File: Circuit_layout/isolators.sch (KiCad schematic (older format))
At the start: 0 parts

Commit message: added isolators, as well as voltage meas circuit used by tim
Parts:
- added C? (x6): 0.1u, symbol C
- added C?: DNP, symbol C
- added R? (x5): 2k, symbol R
- added R? (x6): 5k, symbol R
- added R?: 3k, symbol R
- added R? (x2): 4k, symbol R
- added R? (x8): 10k, symbol R
- added R?: 1400, symbol R
- added U? (x3): ACPL-C870, symbol ACPL-C870
- added U? (x3): MCP6004, symbol MCP6004
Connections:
- net labels added: +5V, +5_HV, GND, HV_RTN
- wire segments 0 -> 84
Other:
- note added: "5/4 scaling due to\n0-4V output of I sensor\nConfirm this O/P"
- note added: "Based on 110V (max) from TSV. Planning on putting voltages ~0-2V.\nWhen scaled, will be roughly ~0-5V for ADC read."
- note added: "current meas iso\n"
- note added: "throttle iso"
- note added: "voltage meas iso\n"

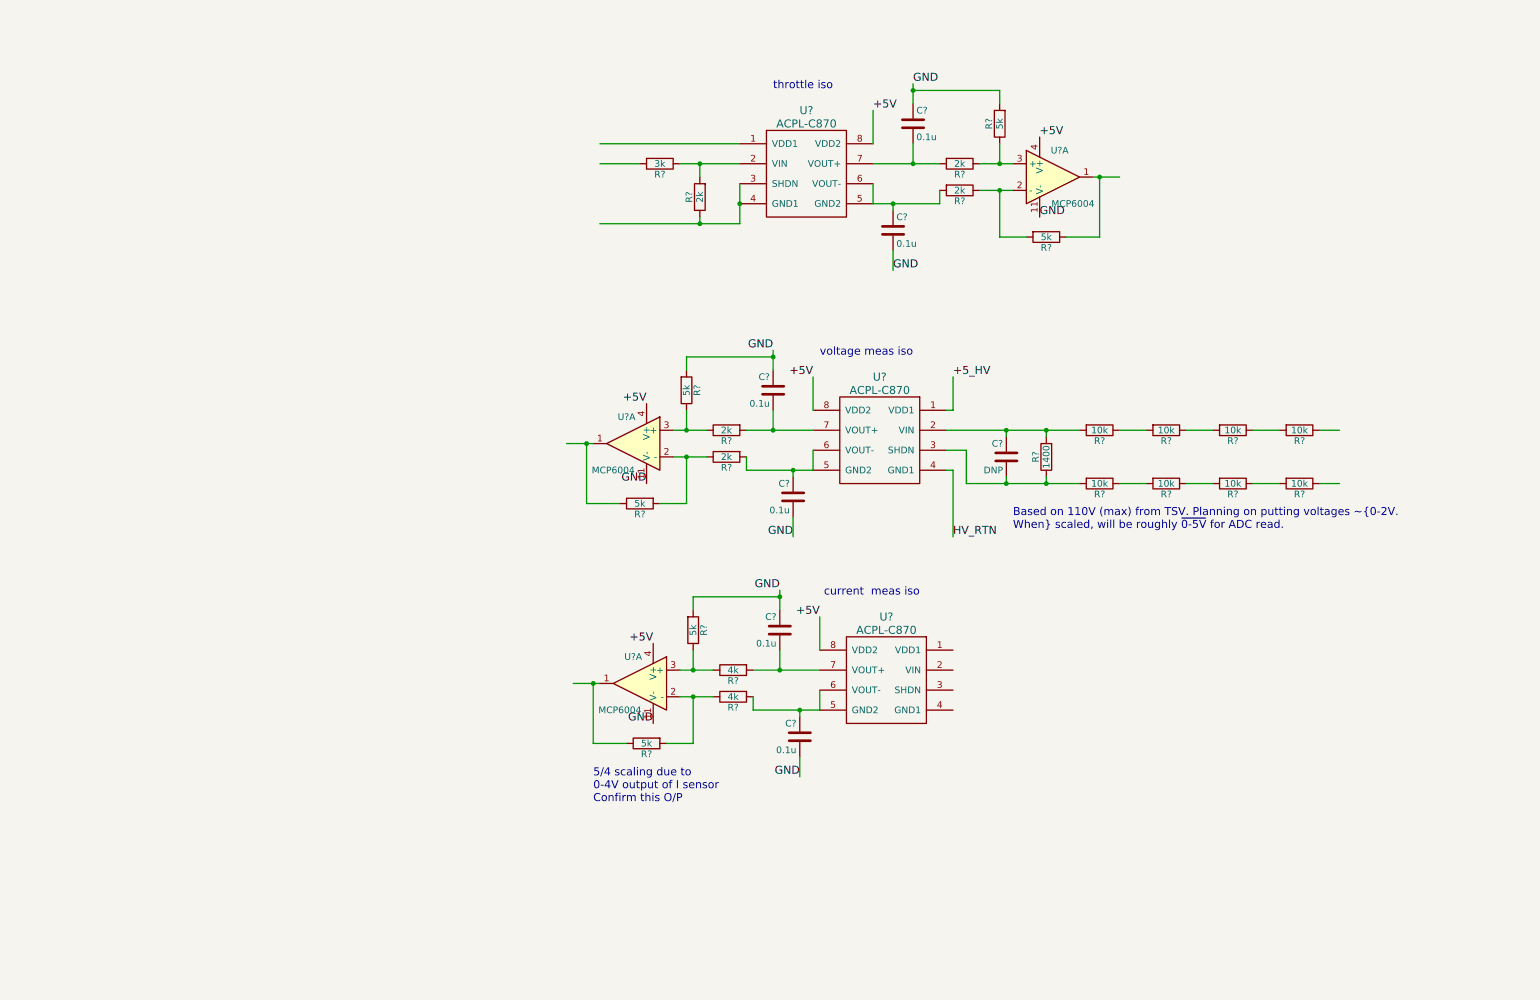
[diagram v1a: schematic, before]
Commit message: added iso circuits, curr. sensor diff amp, IMD fault lt circuit, updated labels
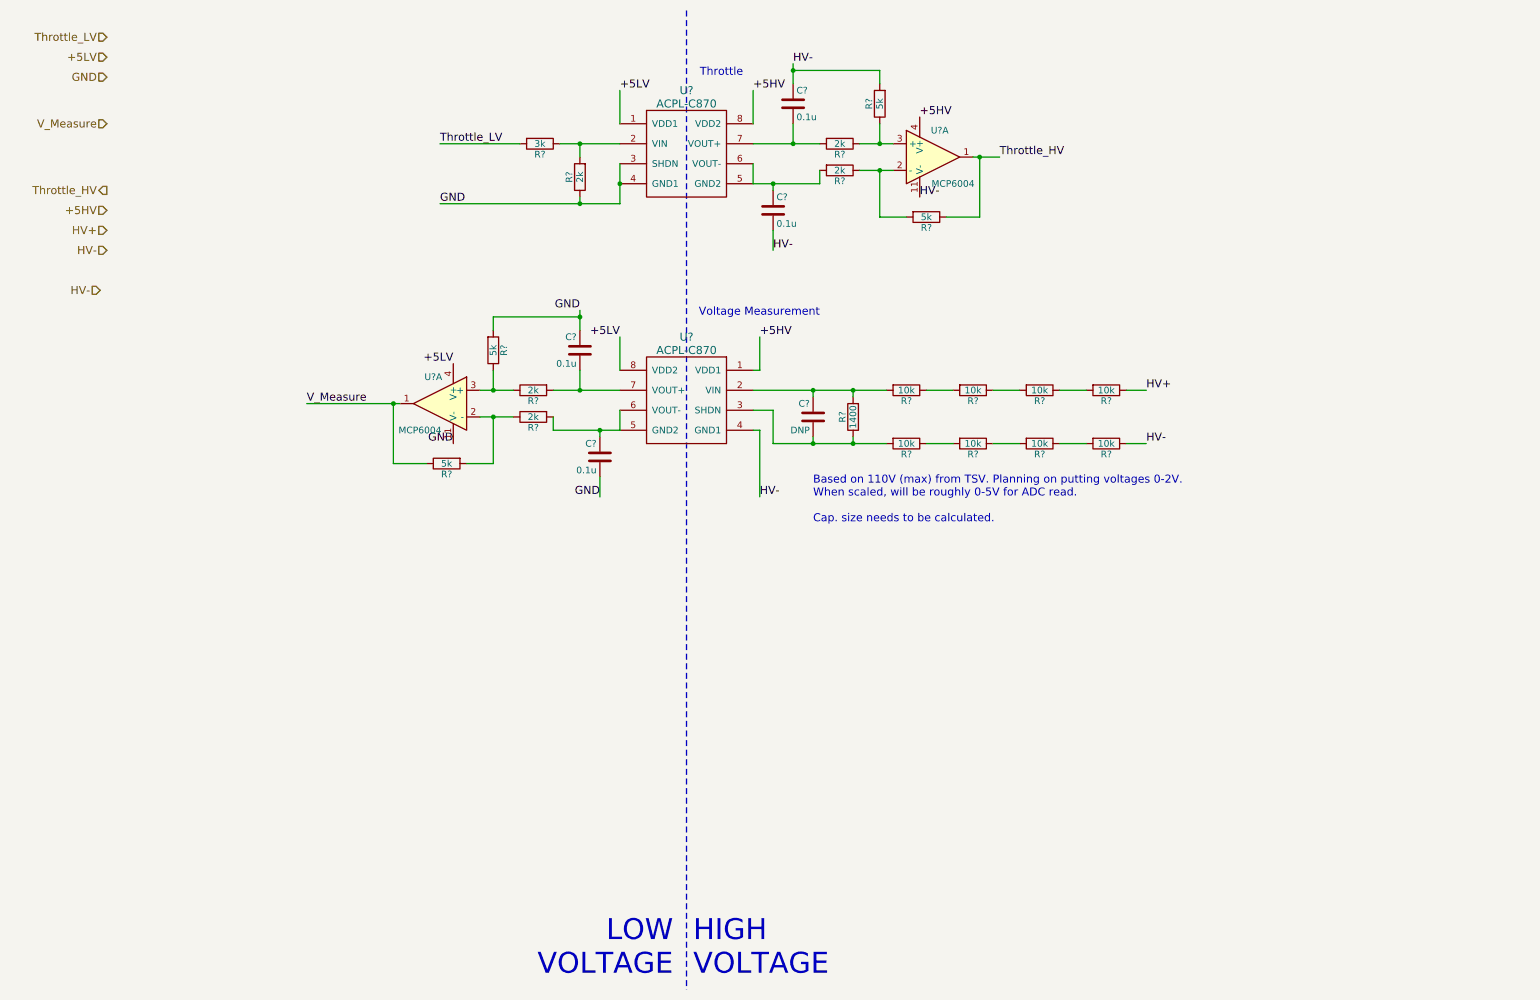
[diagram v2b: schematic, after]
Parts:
- removed C? (x2): 0.1u, symbol C
- removed R? (x2): 4k, symbol R
- removed R? (x2): 5k, symbol R
- removed U?: ACPL-C870, symbol ACPL-C870
- removed U?: MCP6004, symbol MCP6004
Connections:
- net labels added: +5HV, +5LV, HV+, HV-, Throttle_HV, Throttle_LV, V_Measure
- net labels removed: +5V, +5_HV, HV_RTN
- wire segments 84 -> 65
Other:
- note added: "Based on 110V (max) from TSV. Planning on putting voltages 0-2V.\nWhen scaled, will be roughly 0-5V for ADC read.\n\nCap. size needs to be calculated."
- note added: "HIGH\nVOLTAGE"
- note added: "LOW\nVOLTAGE"
- note added: "Throttle"
- note added: "Voltage Measurement"
- note removed: "5/4 scaling due to\n0-4V output of I sensor\nConfirm this O/P"
- note removed: "Based on 110V (max) from TSV. Planning on putting voltages ~0-2V.\nWhen scaled, will be roughly ~0-5V for ADC read."
- note removed: "current meas iso\n"
- note removed: "throttle iso"
- note removed: "voltage meas iso\n"
- moved on the sheet: C?, R?, U?, U?A

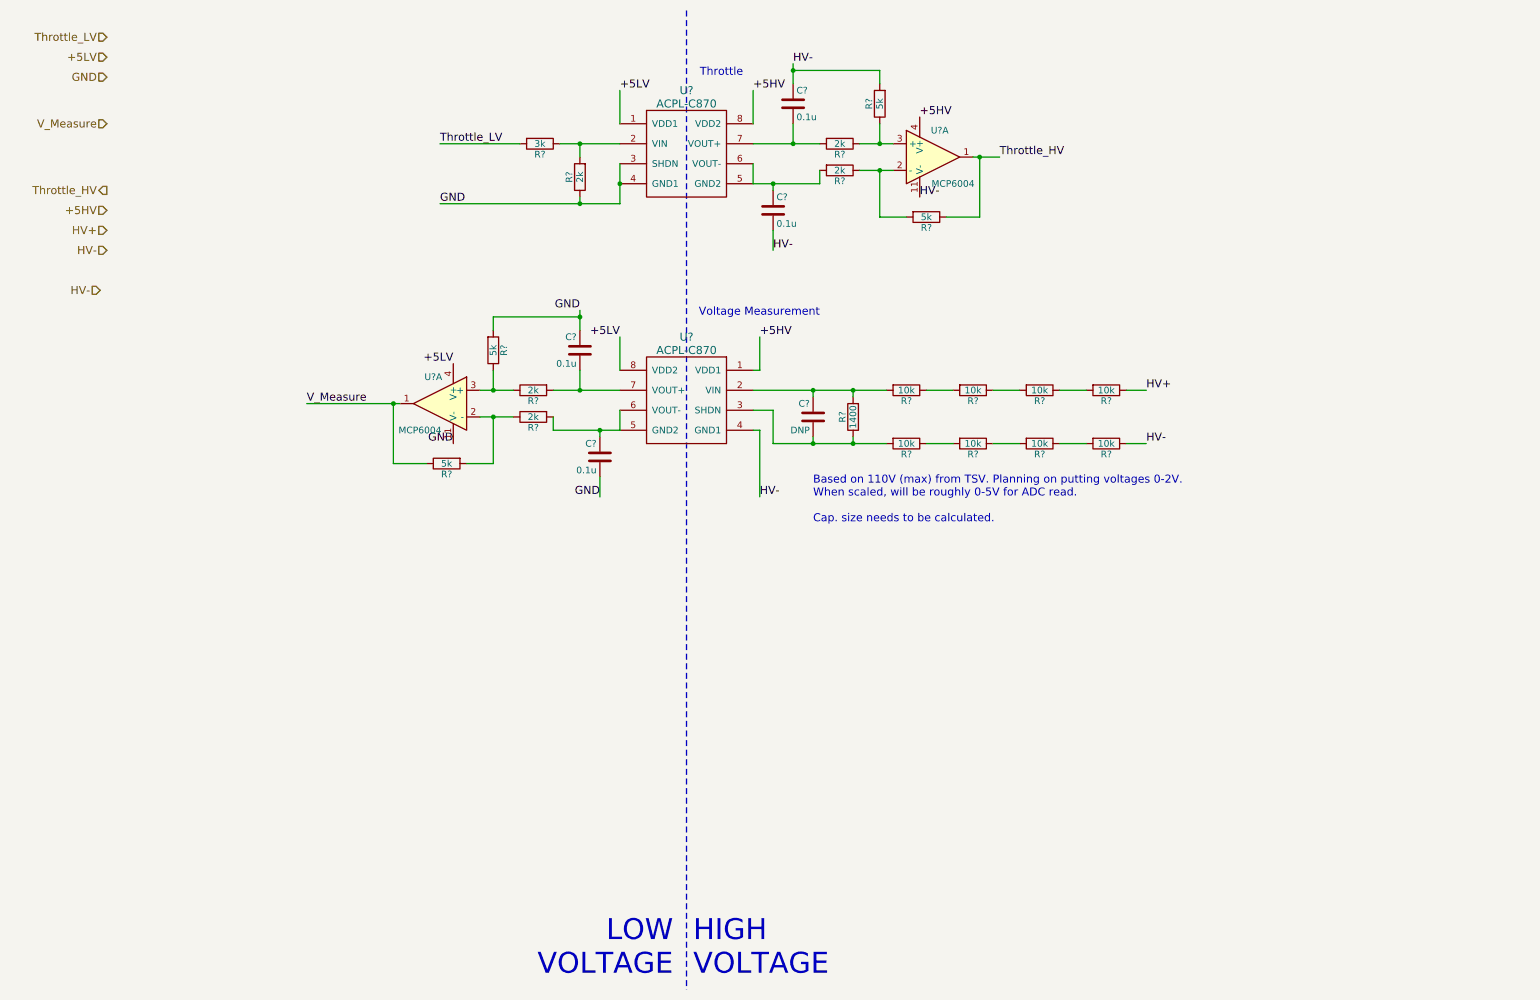
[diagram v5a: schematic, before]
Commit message: filling out field info. for all added devices. think im done w/ resistors.
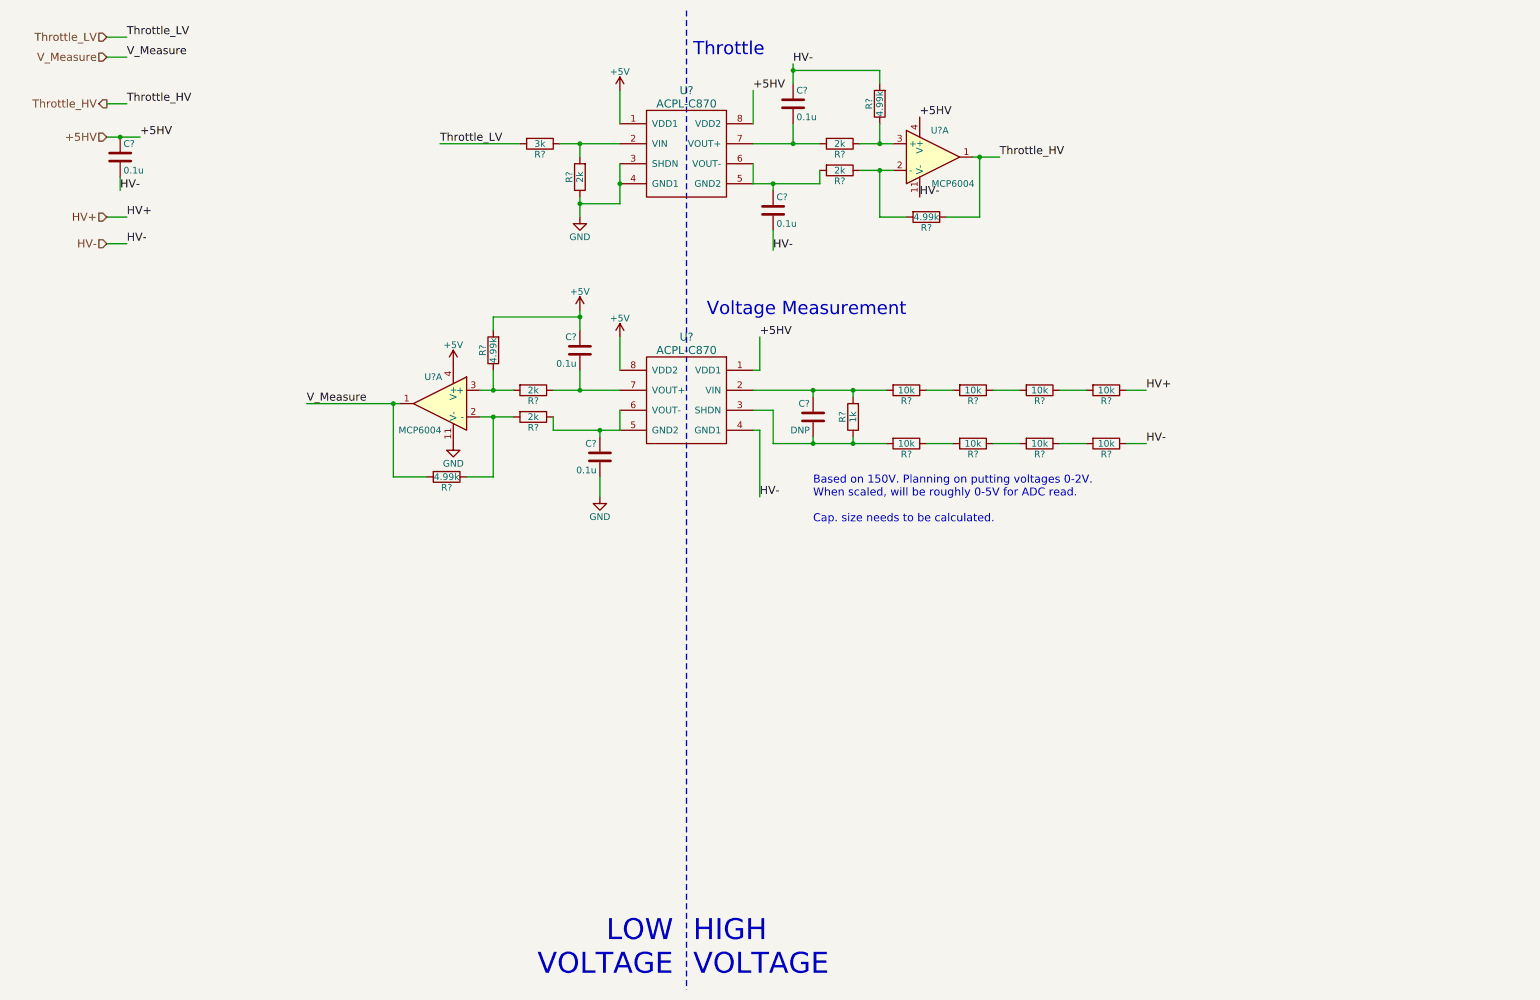
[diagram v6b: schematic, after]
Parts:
- removed R? (x5): 2k, symbol R
- removed R? (x4): 5k, symbol R
- removed R?: 3k, symbol R
- removed R? (x8): 10k, symbol R
- removed R?: 1400, symbol R
- added C?: 0.1u, symbol C
- added R? (x8): 10k, Resistors_SMD:R_0805_HandSoldering, symbol R
- added R?: 1k, Resistors_SMD:R_0805_HandSoldering, symbol R
- added R? (x4): 4.99k, Resistors_SMD:R_0805_HandSoldering, symbol R
- added R? (x5): 2k, Resistors_SMD:R_0805_HandSoldering, symbol R
- added R?: 3k, Resistors_SMD:R_0805_HandSoldering, symbol R
- C?: footprint (none) -> Capacitors_SMD:C_0805_HandSoldering
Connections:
- net +5HV: now also C?.1
- net GND: now also R?.1; no longer C?.1
- net HV+: now also R?.1
- net HV-: now also C?.2, R?.1, R?.2
- net Throttle_HV: now also R?.1
- net Throttle_LV: now also R?.2
- net V_Measure: now also R?.2
- net at U?.2 (VIN): now also R?.1, R?.2
- net at C?.1, U?.5 (GND2), U?.6 (VOUT-): now also R?.2
- net at C?.2, U?.7 (VOUT+): now also R?.2
- net at U?.2 (-): now also R?.1, R?.2 (x2)
- net at U?.3 (+): now also R?.1, R?.1
- net at C?.1, U?.2 (VIN): now also R?.2, R?.2
- net at C?.2, U?.3 (SHDN): now also R?.1, R?.2
- net at C?.1, U?.5 (GND2), U?.6 (VOUT-): now also R?.1
- net at C?.2, U?.7 (VOUT+): now also R?.1
- net at U?.3 (+): now also R?.1, R?.2
- net +5LV renamed +5V
- net +5V: now also C?.1, R?.2
- new net: R?.1, R?.2 (x6)
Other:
- note added: "Based on 150V. Planning on putting voltages 0-2V.\nWhen scaled, will be roughly 0-5V for ADC read.\n\nCap. size needs to be calculated."
- note removed: "Based on 110V (max) from TSV. Planning on putting voltages 0-2V.\nWhen scaled, will be roughly 0-5V for ADC read.\n\nCap. size needs to be calculated."

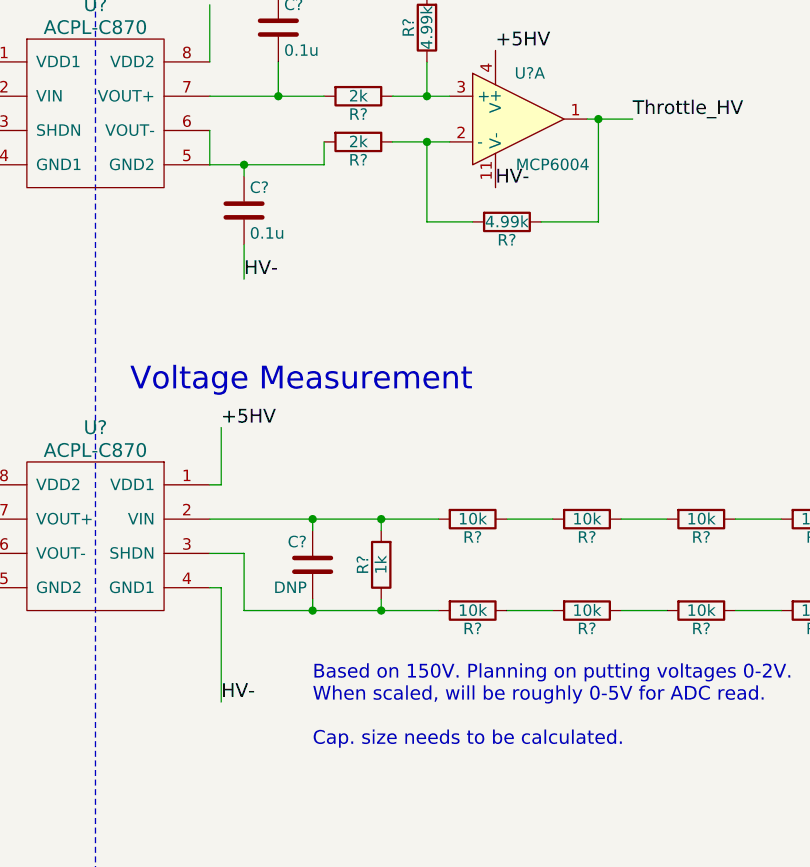
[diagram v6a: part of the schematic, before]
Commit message: added cap. info. for orders
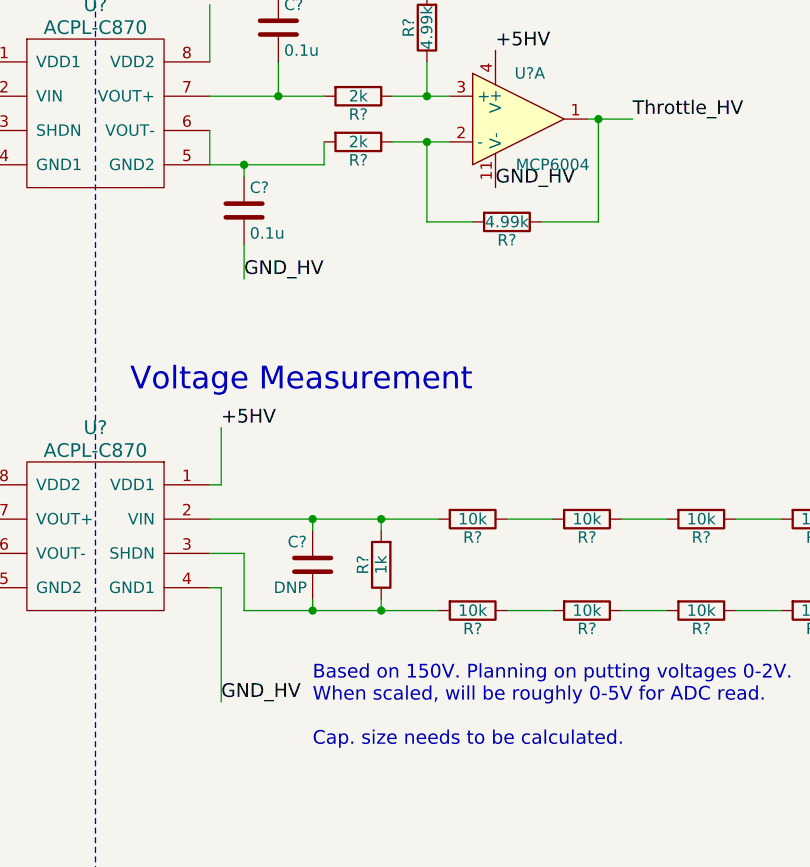
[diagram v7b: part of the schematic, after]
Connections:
- net HV-: no longer C?.2, U?.11 (V-), U?.4 (GND1)
- new net GND_HV: C?.2, U?.11 (V-), U?.4 (GND1)
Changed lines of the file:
@@
 EESchema Schematic File Version 2
 LIBS:Circuit_layout-rescue
-LIBS:TSI_KiCad_Lib
 LIBS:TSI_HV_Isolater-cache
 LIBS:74xgxx
@@
 +5HV
 Text Label 7200 1850 0    60   ~ 0
-HV-
+GND_HV
 Text Label 6250 850  0    60   ~ 0
 HV-
@@
 $EndComp
 Text Label 6100 2250 0    60   ~ 0
-HV-
+GND_HV
 Wire Wire Line
 	6900 2000 6900 1650
@@
 $EndComp
 Text Label 6000 4100 0    60   ~ 0
-HV-
+GND_HV
 Wire Wire Line
 	5950 3600 6000 3600
